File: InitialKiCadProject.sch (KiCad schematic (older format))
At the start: 0 parts

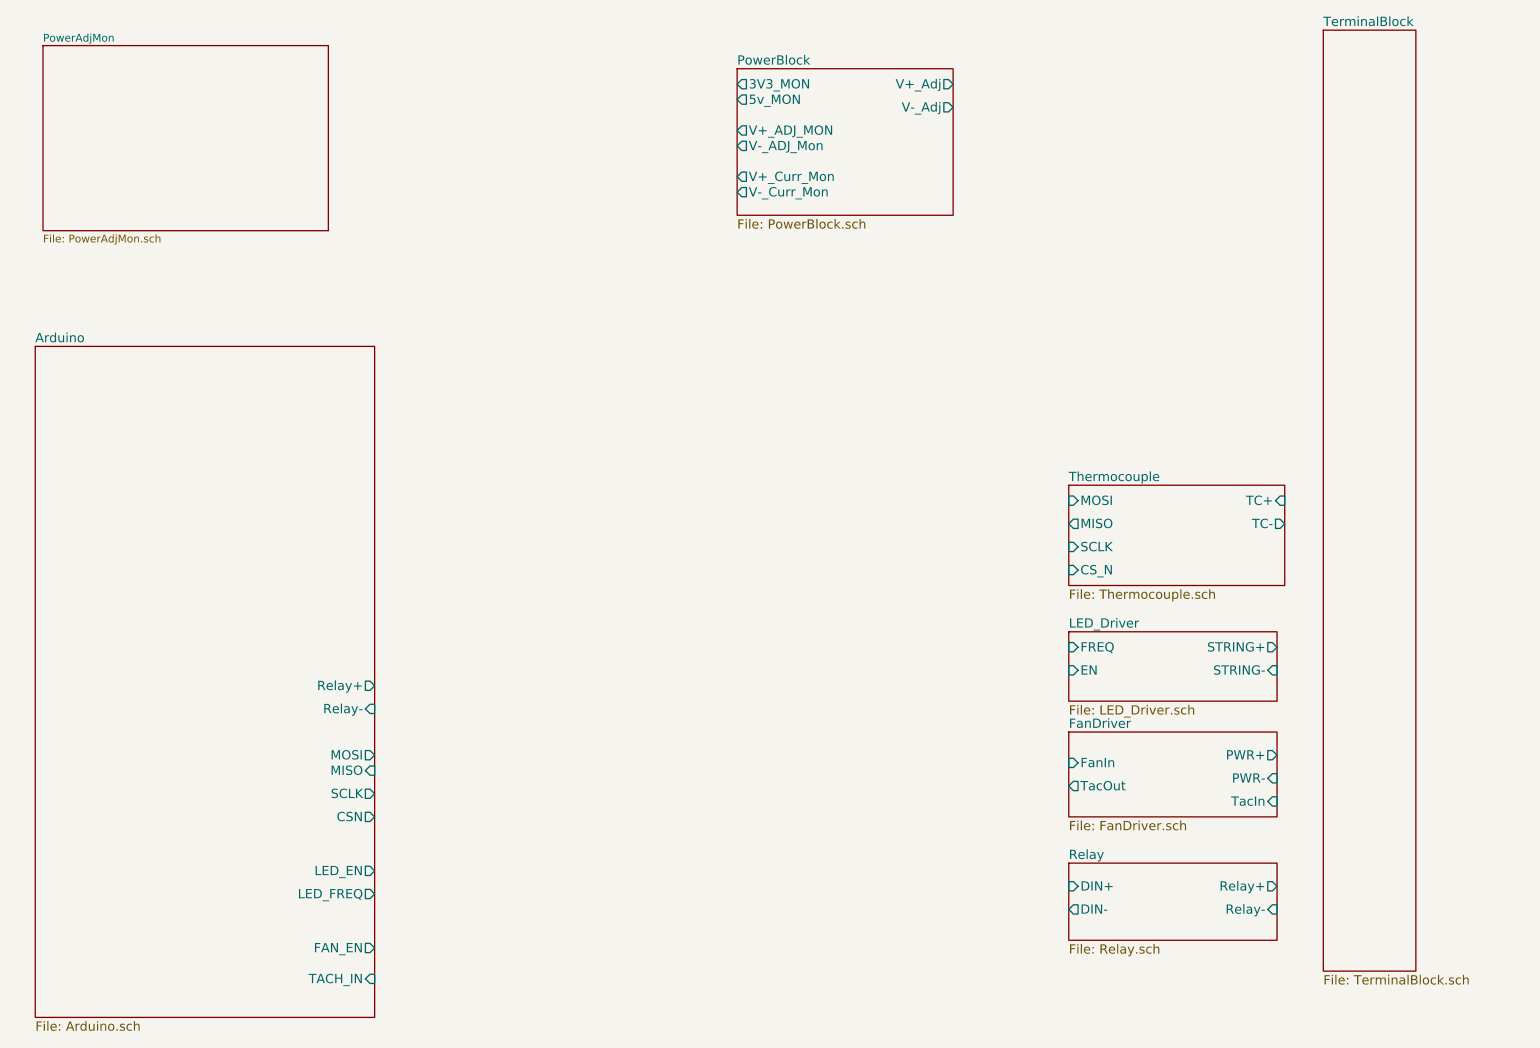
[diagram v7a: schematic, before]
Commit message: WIRED BLOCK DIAGRAM TOGETHER AND ADDED ARDUINO BLOCK
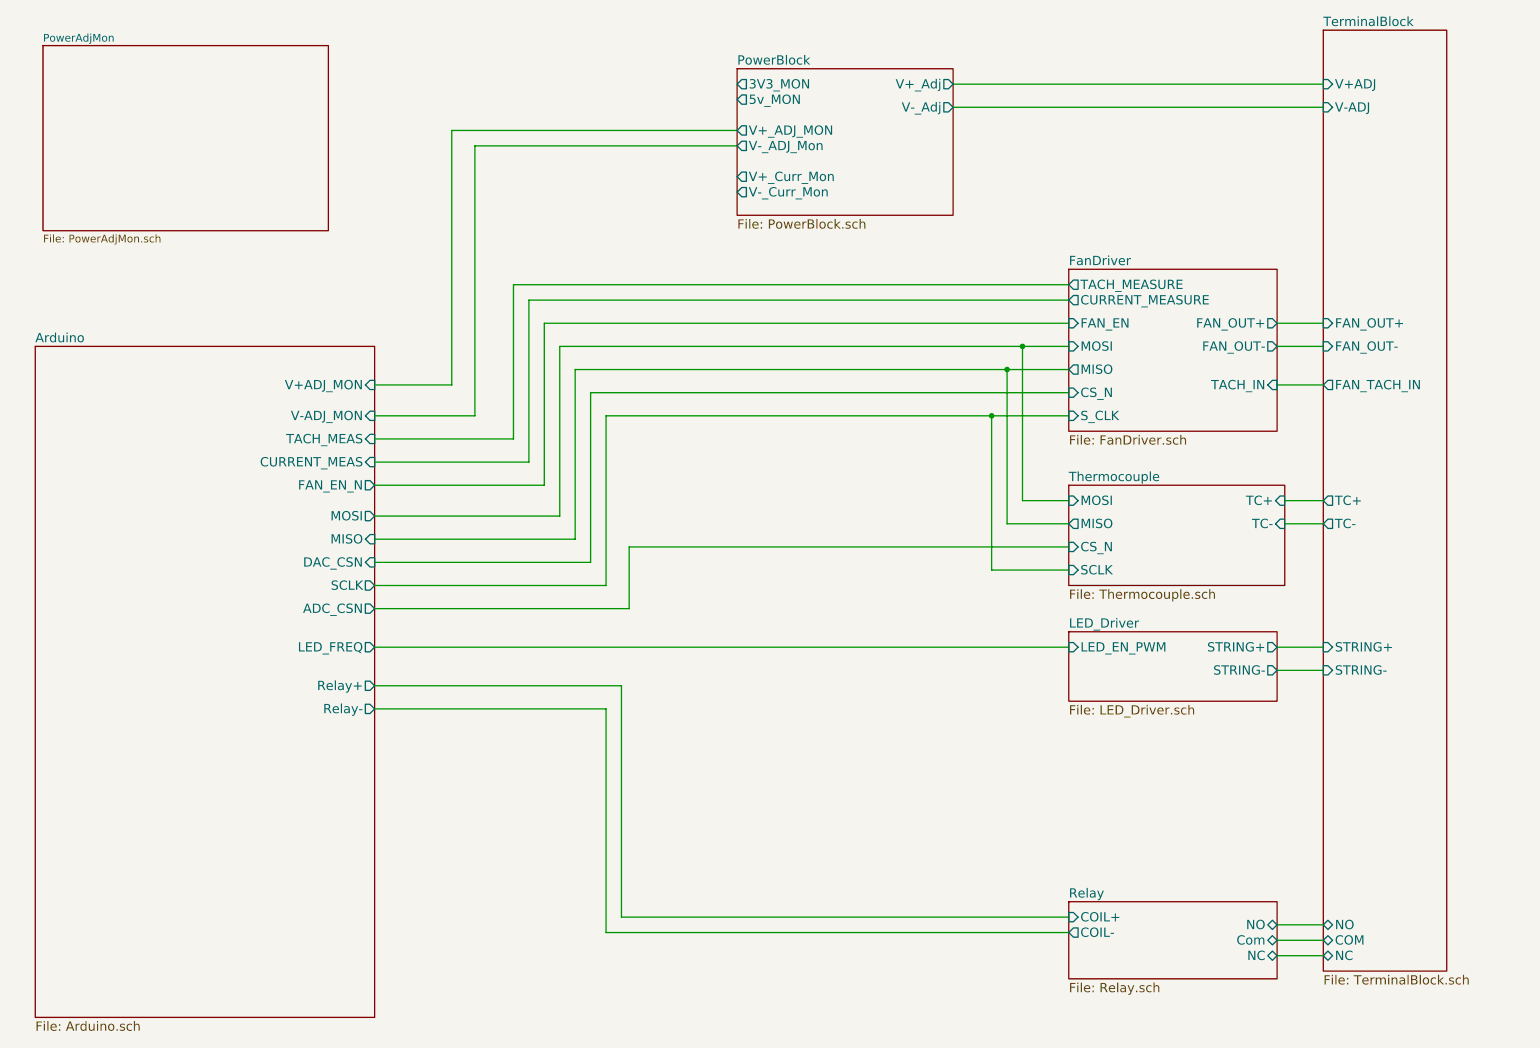
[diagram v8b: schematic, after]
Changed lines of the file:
@@
-EESchema Schematic File Version 2  date Sat 08 Feb 2014 08:25:16 PM EST
+EESchema Schematic File Version 2  date Sat 08 Feb 2014 11:37:49 PM EST
 LIBS:power
 LIBS:device
@@
 Comment4 ""
 $EndDescr
+Wire Wire Line
+	9900 3200 10200 3200
+Wire Wire Line
+	9900 2800 10200 2800
+Wire Wire Line
+	8550 6750 5550 6750
+Wire Wire Line
+	5550 6750 5550 5300
+Wire Wire Line
+	5550 5300 4050 5300
+Wire Wire Line
+	4050 4500 5550 4500
+Connection ~ 8050 3400
+Wire Wire Line
+	8050 3400 8050 4400
+Wire Wire Line
+	8050 4400 8550 4400
+Connection ~ 8250 2950
+Wire Wire Line
+	8250 2950 8250 3950
+Wire Wire Line
+	8250 3950 8550 3950
+Wire Wire Line
+	8550 3250 5450 3250
+Wire Wire Line
+	5450 3250 5450 4350
+Wire Wire Line
+	5450 4350 4050 4350
+Wire Wire Line
+	8550 2950 5250 2950
+Wire Wire Line
+	5250 2950 5250 4050
+Wire Wire Line
+	5250 4050 4050 4050
+Wire Wire Line
+	4050 3700 5050 3700
+Wire Wire Line
+	5050 3700 5050 2650
+Wire Wire Line
+	8550 2550 4950 2550
+Wire Wire Line
+	4950 2550 4950 3550
+Wire Wire Line
+	4950 3550 4050 3550
+Wire Wire Line
+	6400 1650 4700 1650
+Wire Wire Line
+	4700 1650 4700 3400
+Wire Wire Line
+	4700 3400 4050 3400
+Wire Wire Line
+	7800 1400 10200 1400
+Wire Wire Line
+	9900 5050 10200 5050
+Wire Wire Line
+	9950 4100 10200 4100
+Wire Wire Line
+	9900 6800 10200 6800
+Wire Wire Line
+	9900 6900 10200 6900
+Wire Wire Line
+	9900 6700 10200 6700
+Wire Wire Line
+	9950 3950 10200 3950
+Wire Wire Line
+	9900 4900 10200 4900
+Wire Wire Line
+	7800 1250 10200 1250
+Wire Wire Line
+	4050 3200 4550 3200
+Wire Wire Line
+	4550 3200 4550 1550
+Wire Wire Line
+	4550 1550 6400 1550
+Wire Wire Line
+	5050 2650 8550 2650
+Wire Wire Line
+	4050 3850 5150 3850
+Wire Wire Line
+	5150 3850 5150 2800
+Wire Wire Line
+	5150 2800 8550 2800
+Wire Wire Line
+	4050 4200 5350 4200
+Wire Wire Line
+	5350 4200 5350 3100
+Wire Wire Line
+	5350 3100 8550 3100
+Wire Wire Line
+	5550 4500 5550 3400
+Wire Wire Line
+	5550 3400 8550 3400
+Wire Wire Line
+	8550 4100 8150 4100
+Wire Wire Line
+	8150 4100 8150 3100
+Connection ~ 8150 3100
+Wire Wire Line
+	4050 4650 5700 4650
+Wire Wire Line
+	5700 4650 5700 4250
+Wire Wire Line
+	5700 4250 8550 4250
+Wire Wire Line
+	4050 4900 8550 4900
+Wire Wire Line
+	4050 5150 5650 5150
+Wire Wire Line
+	5650 5150 5650 6650
+Wire Wire Line
+	5650 6650 8550 6650
+Wire Wire Line
+	9900 2950 10200 2950
+$Sheet
+S 8550 3850 1400 650
+U 52F1B638
+F0 "Thermocouple" 60
+F1 "Thermocouple.sch" 60
+F2 "TC+" I R 9950 3950 60
+F3 "CS_N" I L 8550 4250 60
+F4 "SCLK" I L 8550 4400 60
+F5 "MISO" O L 8550 4100 60
+F6 "MOSI" I L 8550 3950 60
+F7 "TC-" I R 9950 4100 60
+$EndSheet
+$Sheet
+S 8550 2450 1350 1050
+U 52F1B6C1
+F0 "FanDriver" 60
+F1 "FanDriver.sch" 60
+F2 "FAN_OUT+" O R 9900 2800 60
+F3 "FAN_EN" I L 8550 2800 60
+F4 "TACH_MEASURE" O L 8550 2550 60
+F5 "TACH_IN" I R 9900 3200 60
+F6 "CURRENT_MEASURE" O L 8550 2650 60
+F7 "MISO" O L 8550 3100 60
+F8 "MOSI" I L 8550 2950 60
+F9 "CS_N" I L 8550 3250 60
+F10 "S_CLK" I L 8550 3400 60
+F11 "FAN_OUT-" O R 9900 2950 60
+$EndSheet
+$Sheet
+S 1850 2950 2200 4350
+U 52F1B5F2
+F0 "Arduino" 60
+F1 "Arduino.sch" 60
+F2 "LED_FREQ" O R 4050 4900 60
+F3 "SCLK" O R 4050 4500 60
+F4 "MISO" I R 4050 4200 60
+F5 "MOSI" O R 4050 4050 60
+F6 "Relay+" O R 4050 5150 60
+F7 "CURRENT_MEAS" I R 4050 3700 60
+F8 "TACH_MEAS" I R 4050 3550 60
+F9 "FAN_EN_N" O R 4050 3850 60
+F10 "Relay-" O R 4050 5300 60
+F11 "V-ADJ_MON" I R 4050 3400 60
+F12 "V+ADJ_MON" I R 4050 3200 60
+F13 "DAC_CSN" I R 4050 4350 60
+F14 "ADC_CSN" O R 4050 4650 60
+$EndSheet
+$Sheet
+S 10200 900  800  6100
+U 52F1B712
+F0 "TerminalBlock" 60
+F1 "TerminalBlock.sch" 60
+F2 "COM" B L 10200 6800 60
+F3 "NC" B L 10200 6900 60
+F4 "NO" B L 10200 6700 60
+F5 "STRING-" I L 10200 5050 60
+F6 "STRING+" I L 10200 4900 60
+F7 "FAN_TACH_IN" O L 10200 3200 60
+F8 "FAN_OUT-" I L 10200 2950 60
+F9 "FAN_OUT+" I L 10200 2800 60
+F10 "TC-" O L 10200 4100 60
+F11 "TC+" O L 10200 3950 60
+F12 "V-ADJ" I L 10200 1400 60
+F13 "V+ADJ" I L 10200 1250 60
+$EndSheet
 $Sheet
 S 8550 4800 1350 450
@@
 F0 "LED_Driver" 60
 F1 "LED_Driver.sch" 60
-F2 "STRING-" I R 9900 5050 60
-F3 "STRING+" O R 9900 4900 60
-F4 "FREQ" I L 8550 4900 60
-F5 "EN" I L 8550 5050 60
-$EndSheet
-$Sheet
-S 10200 900  600  6100
-U 52F1B712
-F0 "TerminalBlock" 60
-F1 "TerminalBlock.sch" 60
-$EndSheet
-$Sheet
-S 8550 5450 1350 550
-U 52F1B6C1
-F0 "FanDriver" 60
-F1 "FanDriver.sch" 60
-F2 "FanIn" I L 8550 5650 60
-F3 "TacOut" O L 8550 5800 60
-F4 "TacIn" I R 9900 5900 60
-F5 "PWR-" I R 9900 5750 60
-F6 "PWR+" O R 9900 5600 60
+F2 "STRING+" O R 9900 4900 60
+F3 "LED_EN_PWM" I L 8550 4900 60
+F4 "STRING-" O R 9900 5050 60
 $EndSheet
 $Sheet
@@
 $EndSheet
 $Sheet
-S 8550 6300 1350 500
+S 8550 6550 1350 500
 U 52F1B673
 F0 "Relay" 60
 F1 "Relay.sch" 60
-F2 "Relay-" I R 9900 6600 60
-F3 "Relay+" O R 9900 6450 60
-F4 "DIN-" O L 8550 6600 60
-F5 "DIN+" I L 8550 6450 60
-$EndSheet
-$Sheet
-S 8550 3850 1400 650
-U 52F1B638
-F0 "Thermocouple" 60
-F1 "Thermocouple.sch" 60
-F2 "TC-" O R 9950 4100 60
-F3 "TC+" I R 9950 3950 60
-F4 "CS_N" I L 8550 4400 60
-F5 "SCLK" I L 8550 4250 60
-F6 "MISO" O L 8550 4100 60
-F7 "MOSI" I L 8550 3950 60
-$EndSheet
-$Sheet
-S 1850 2950 2200 4350
-U 52F1B5F2
-F0 "Arduino" 60
-F1 "Arduino.sch" 60
-F2 "TACH_IN" I R 4050 7050 60
-F3 "FAN_EN" O R 4050 6850 60
-F4 "LED_FREQ" O R 4050 6500 60
-F5 "LED_EN" O R 4050 6350 60
-F6 "CSN" O R 4050 6000 60
-F7 "SCLK" O R 4050 5850 60
-F8 "MISO" I R 4050 5700 60
-F9 "MOSI" O R 4050 5600 60
-F10 "Relay-" I R 4050 5300 60
-F11 "Relay+" O R 4050 5150 60
-$EndSheet
-$Sheet
+F2 "NO" B R 9900 6700 60
+F3 "NC" B R 9900 6900 60
+F4 "Com" B R 9900 6800 60
+F5 "COIL-" O L 8550 6750 60
+F6 "COIL+" I L 8550 6650 60
+$EndSheet
+$Sheet
